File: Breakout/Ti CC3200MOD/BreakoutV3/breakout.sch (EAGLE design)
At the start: 29 parts, among them U1 TPS63001DRCT, U11 XL

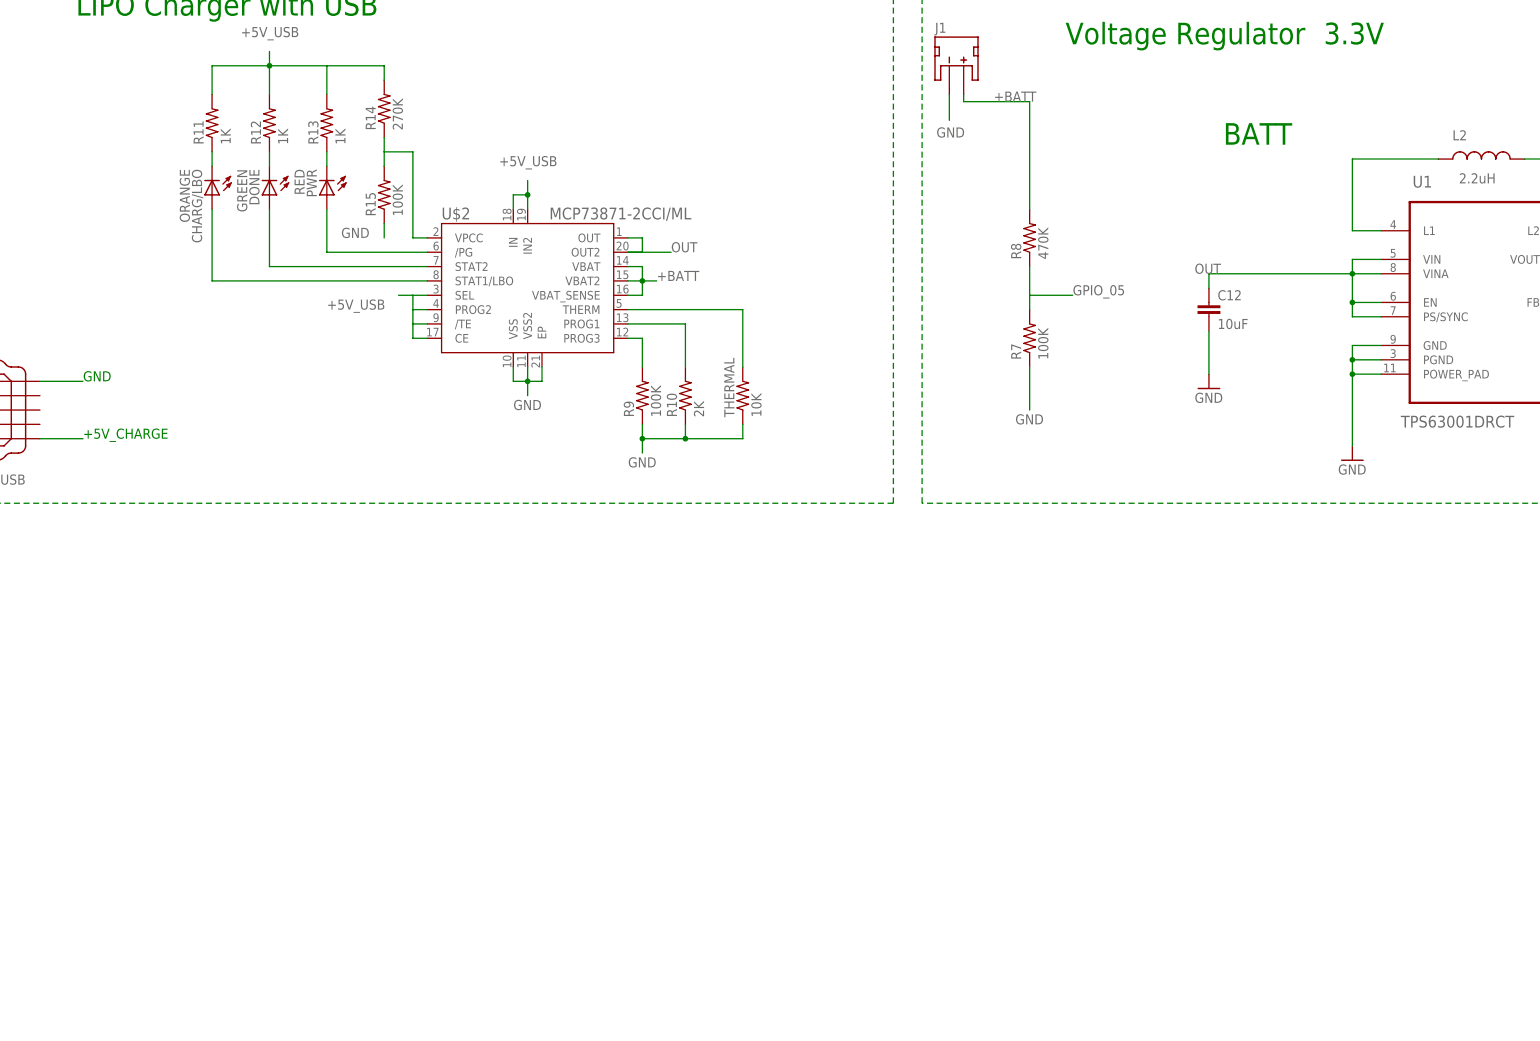
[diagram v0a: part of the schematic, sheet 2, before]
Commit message: added accelormeter
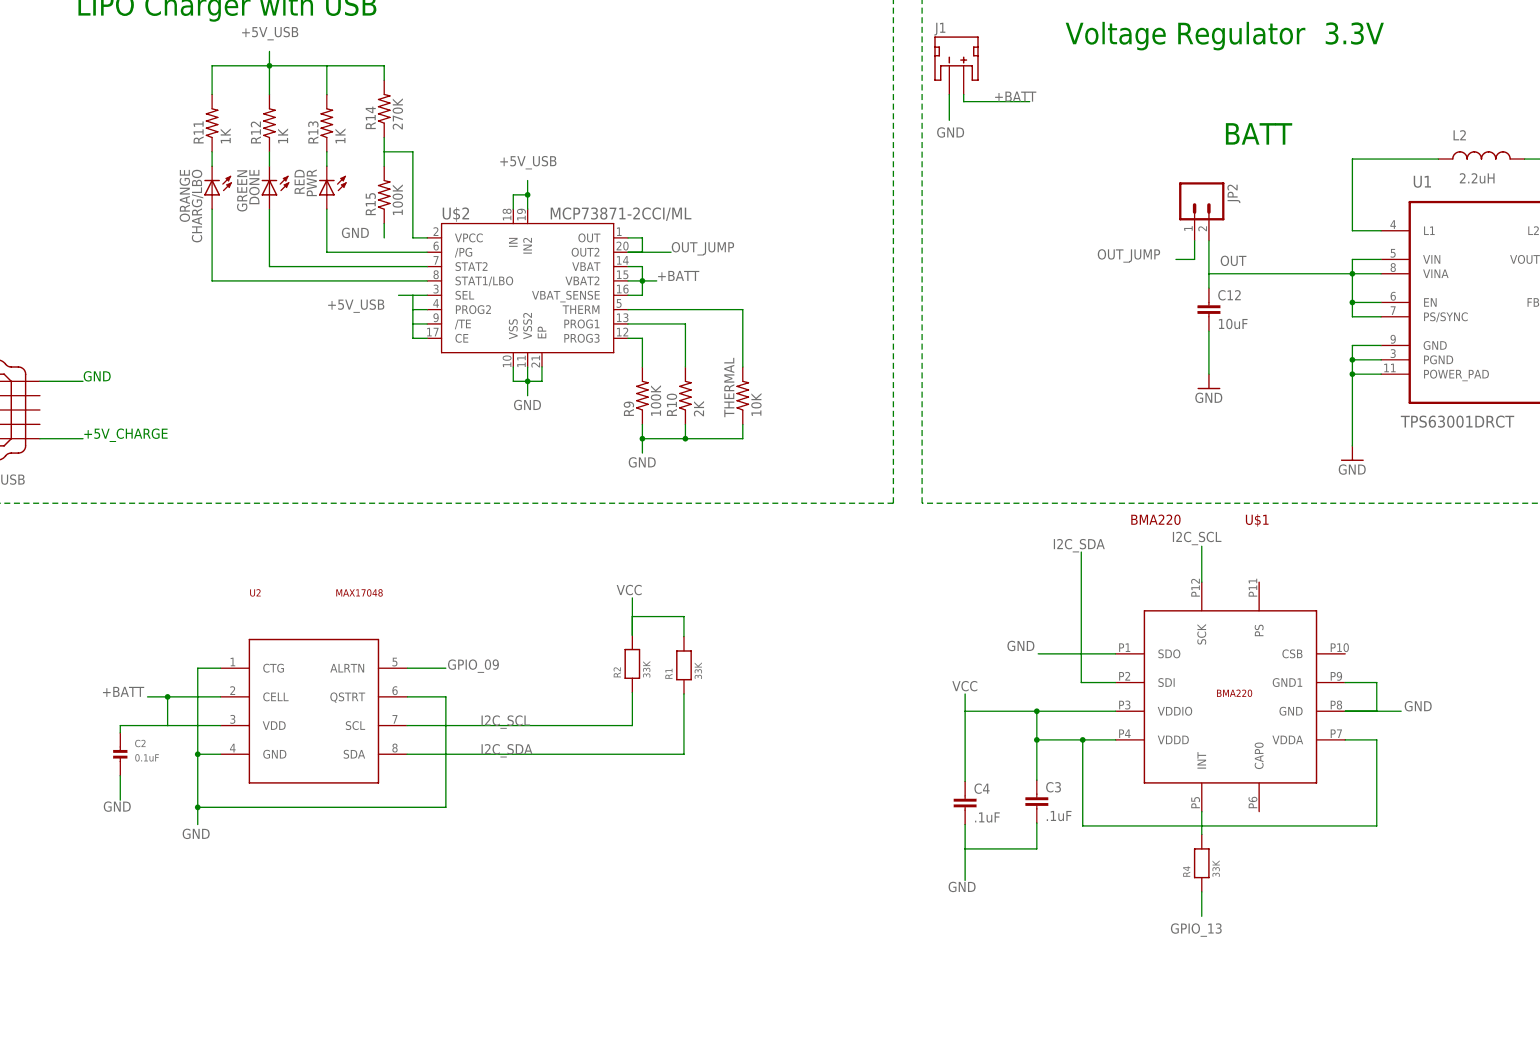
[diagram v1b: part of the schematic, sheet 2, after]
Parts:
- removed JTAG: (no value), con-lstb:MA06-1
- removed R7: 100K, SparkFun-Resistors:RESISTOR0603
- removed R8: 470K, SparkFun-Resistors:RESISTOR0603
- added C2: 0.1uF, microbuilder:CAP_CERAMIC0402
- added C3, C4: .1uF, rcl:C-EUC0603
- added JP2: (no value), DECADE-libraries:M02PTH
- added R1, R2, R4: 33K, microbuilder:RESISTOR0402
- added U$1: BMA220, bma220:BMA220
- added U2: MAX17048, Maxim_By_element14_Batch_1:MAX17048
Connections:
- removed net JTAG_TCK: CC3200MOD.21_JTAG_TCK, JTAG.5
- removed net JTAG_TMS: CC3200MOD.22_JTAP_TMS, JTAG.6
- removed net N$15: CC3200MOD.3_GPIO10, U11.GPIO_10_I2C_SCL
- removed net N$16: CC3200MOD.4_GPIO11, U11.GPIO_11_I2C_SDA
- removed net N$23: CC3200MOD.54_GPIO9, U11.GPIO_09
- new net GPIO_09: CC3200MOD.54_GPIO9, U11.GPIO_09, U2.ALRTN
- new net GPIO_13: R4.1
- new net I2C_SCL: CC3200MOD.3_GPIO10, R2.1, U$1.SCK, U11.GPIO_10_I2C_SCL, U2.SCL
- new net I2C_SDA: CC3200MOD.4_GPIO11, R1.1, U$1.SDI, U11.GPIO_11_I2C_SDA, U2.SDA
- new net N$7: R4.2, U$1.INT
- new net OUT_JUMP: JP2.1, U$2.OUT, U$2.OUT2
- net +BATT: now also C2.P$1, U2.CELL, U2.VDD; no longer R8.2
- net GND: now also C2.P$2, C3.2, C4.2, U$1.GND, U$1.GND1, U$1.SDO, U2.CTG, U2.GND, U2.QSTRT; no longer JTAG.1, R7.1
- net GPIO_05: no longer R7.2, R8.1
- net JTAG_TDI: no longer JTAG.3
- net JTAG_TDO: no longer JTAG.4
- net OUT: now also JP2.2; no longer U$2.OUT, U$2.OUT2
- net VCC: now also C3.1, C4.1, R1.2, R2.2, U$1.VDDA, U$1.VDDD, U$1.VDDIO; no longer JTAG.2

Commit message: Fixed some grounds
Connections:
- net GND: now also U2.EP
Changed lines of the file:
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@@
 <setting verticaltext="up"/>
 </settings>
-<grid distance="0.1" unitdist="inch" unit="inch" style="lines" multiple="1" display="no" altdistance="0.01" altunitdist="inch" altunit="inch"/>
+<grid distance="0.01" unitdist="inch" unit="inch" style="lines" multiple="1" display="no" altdistance="0.01" altunitdist="inch" altunit="inch"/>
 <layers>
 <layer number="1" name="Top" color="4" fill="1" visible="no" active="no"/>
@@
 <segment>
 <wire x1="70.104" y1="373.38" x2="66.04" y2="373.38" width="0.1524" layer="91"/>
-<wire x1="66.04" y1="373.38" x2="66.04" y2="363.982" width="0.1524" layer="91"/>
-<label x="63.246" y="358.394" size="1.778" layer="95"/>
+<wire x1="66.04" y1="373.38" x2="66.04" y2="353.822" width="0.1524" layer="91"/>
+<label x="63.246" y="348.234" size="1.778" layer="95"/>
 <pinref part="U2" gate="G$1" pin="QSTRT"/>
-<wire x1="66.04" y1="363.982" x2="66.04" y2="360.934" width="0.1524" layer="91"/>
+<wire x1="66.04" y1="353.822" x2="66.04" y2="350.774" width="0.1524" layer="91"/>
 <wire x1="103.124" y1="383.54" x2="109.982" y2="383.54" width="0.1524" layer="91"/>
-<wire x1="109.982" y1="383.54" x2="109.982" y2="363.982" width="0.1524" layer="91"/>
-<wire x1="109.982" y1="363.982" x2="66.04" y2="363.982" width="0.1524" layer="91"/>
-<junction x="66.04" y="363.982"/>
+<wire x1="109.982" y1="383.54" x2="109.982" y2="353.822" width="0.1524" layer="91"/>
+<wire x1="109.982" y1="353.822" x2="85.344" y2="353.822" width="0.1524" layer="91"/>
+<junction x="66.04" y="353.822"/>
 <pinref part="U2" gate="G$1" pin="GND"/>
 <pinref part="U2" gate="G$1" pin="CTG"/>
+<wire x1="85.344" y1="353.822" x2="66.04" y2="353.822" width="0.1524" layer="91"/>
 <wire x1="70.104" y1="388.62" x2="66.04" y2="388.62" width="0.1524" layer="91"/>
 <wire x1="66.04" y1="388.62" x2="66.04" y2="373.38" width="0.1524" layer="91"/>
 <junction x="66.04" y="373.38"/>
-</segment>
-<segment>
+<pinref part="U2" gate="G$1" pin="EP"/>
+<wire x1="85.344" y1="363.22" x2="85.344" y2="353.822" width="0.1524" layer="91"/>
+<junction x="85.344" y="353.822"/>
+</segment>
+<segment>
